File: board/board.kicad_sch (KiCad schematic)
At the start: 8 parts, among them J1 020_1000BASE-T_with_CT, J2 003_power, J3 008_USB, J4 001_I2C, J5 008_USB, J6 002_SPI, J7 010_UART

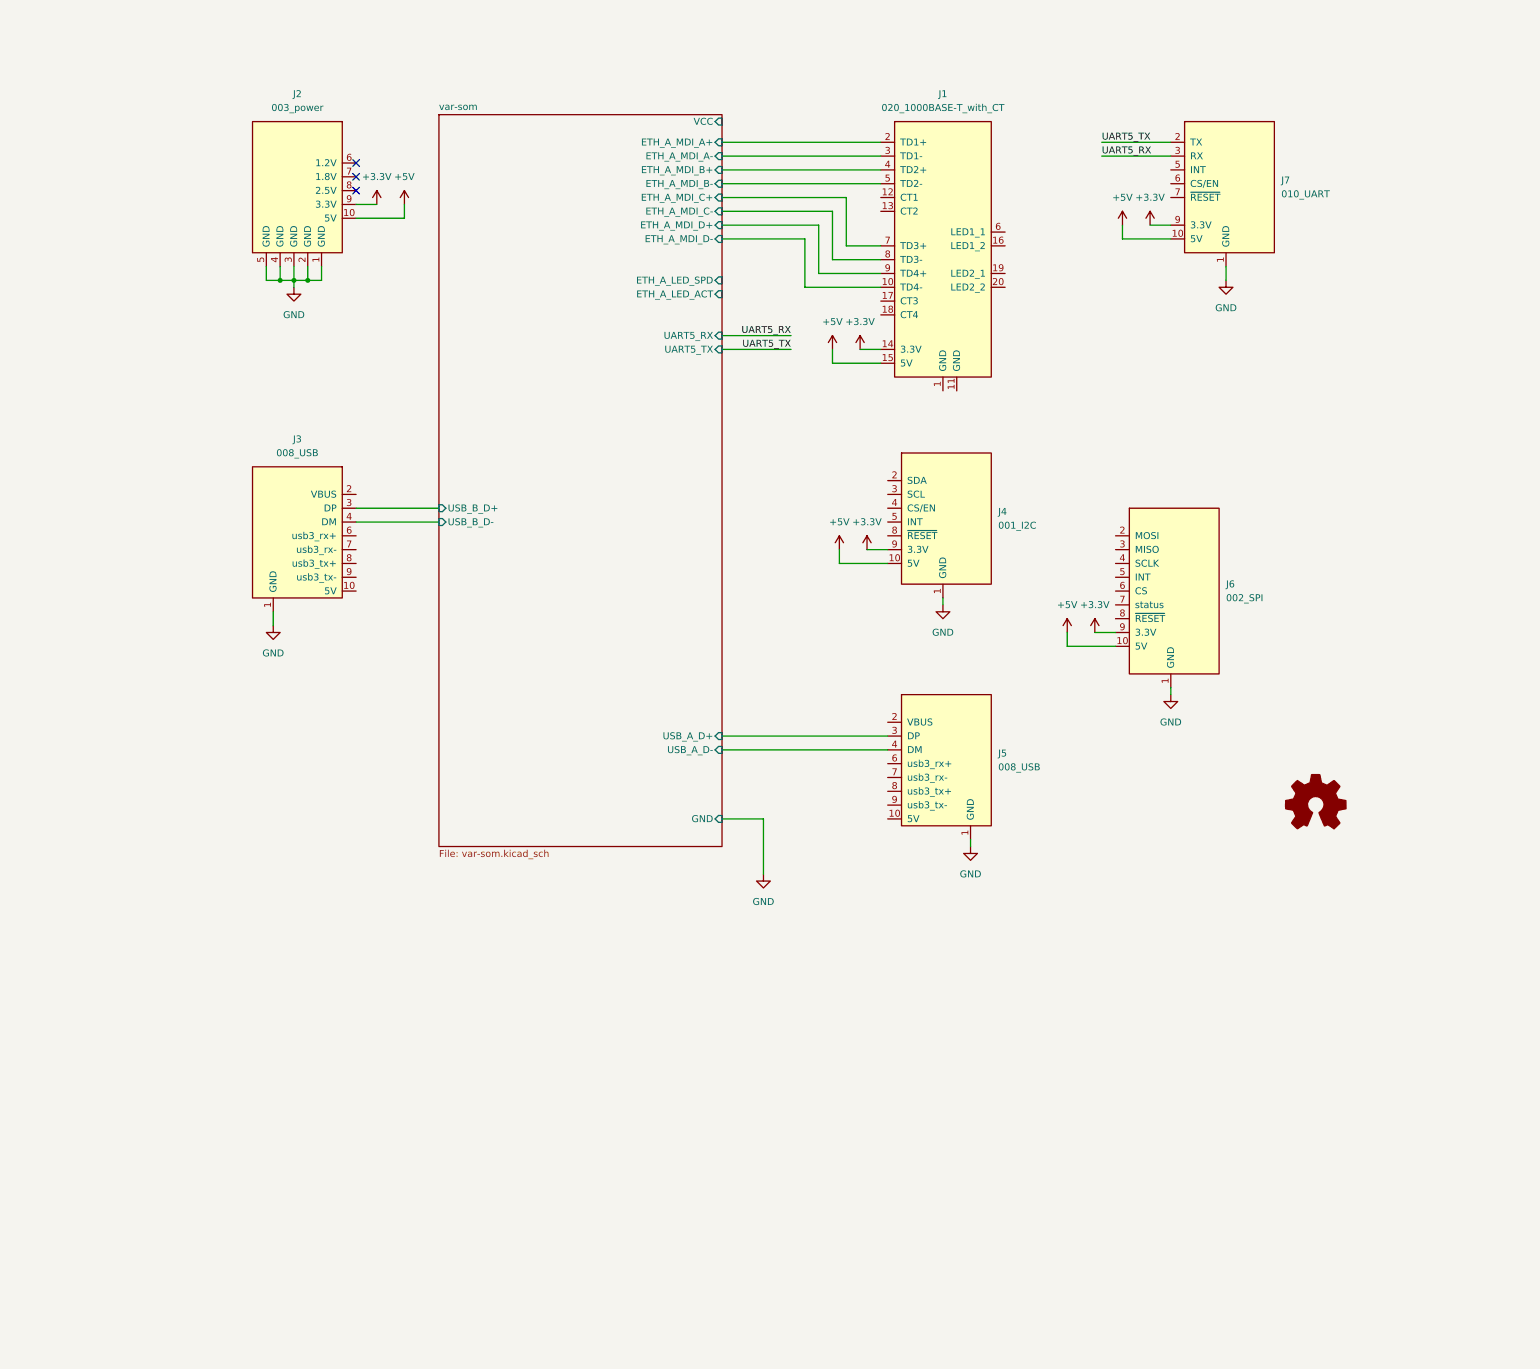
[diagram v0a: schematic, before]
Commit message: added RGMII interface
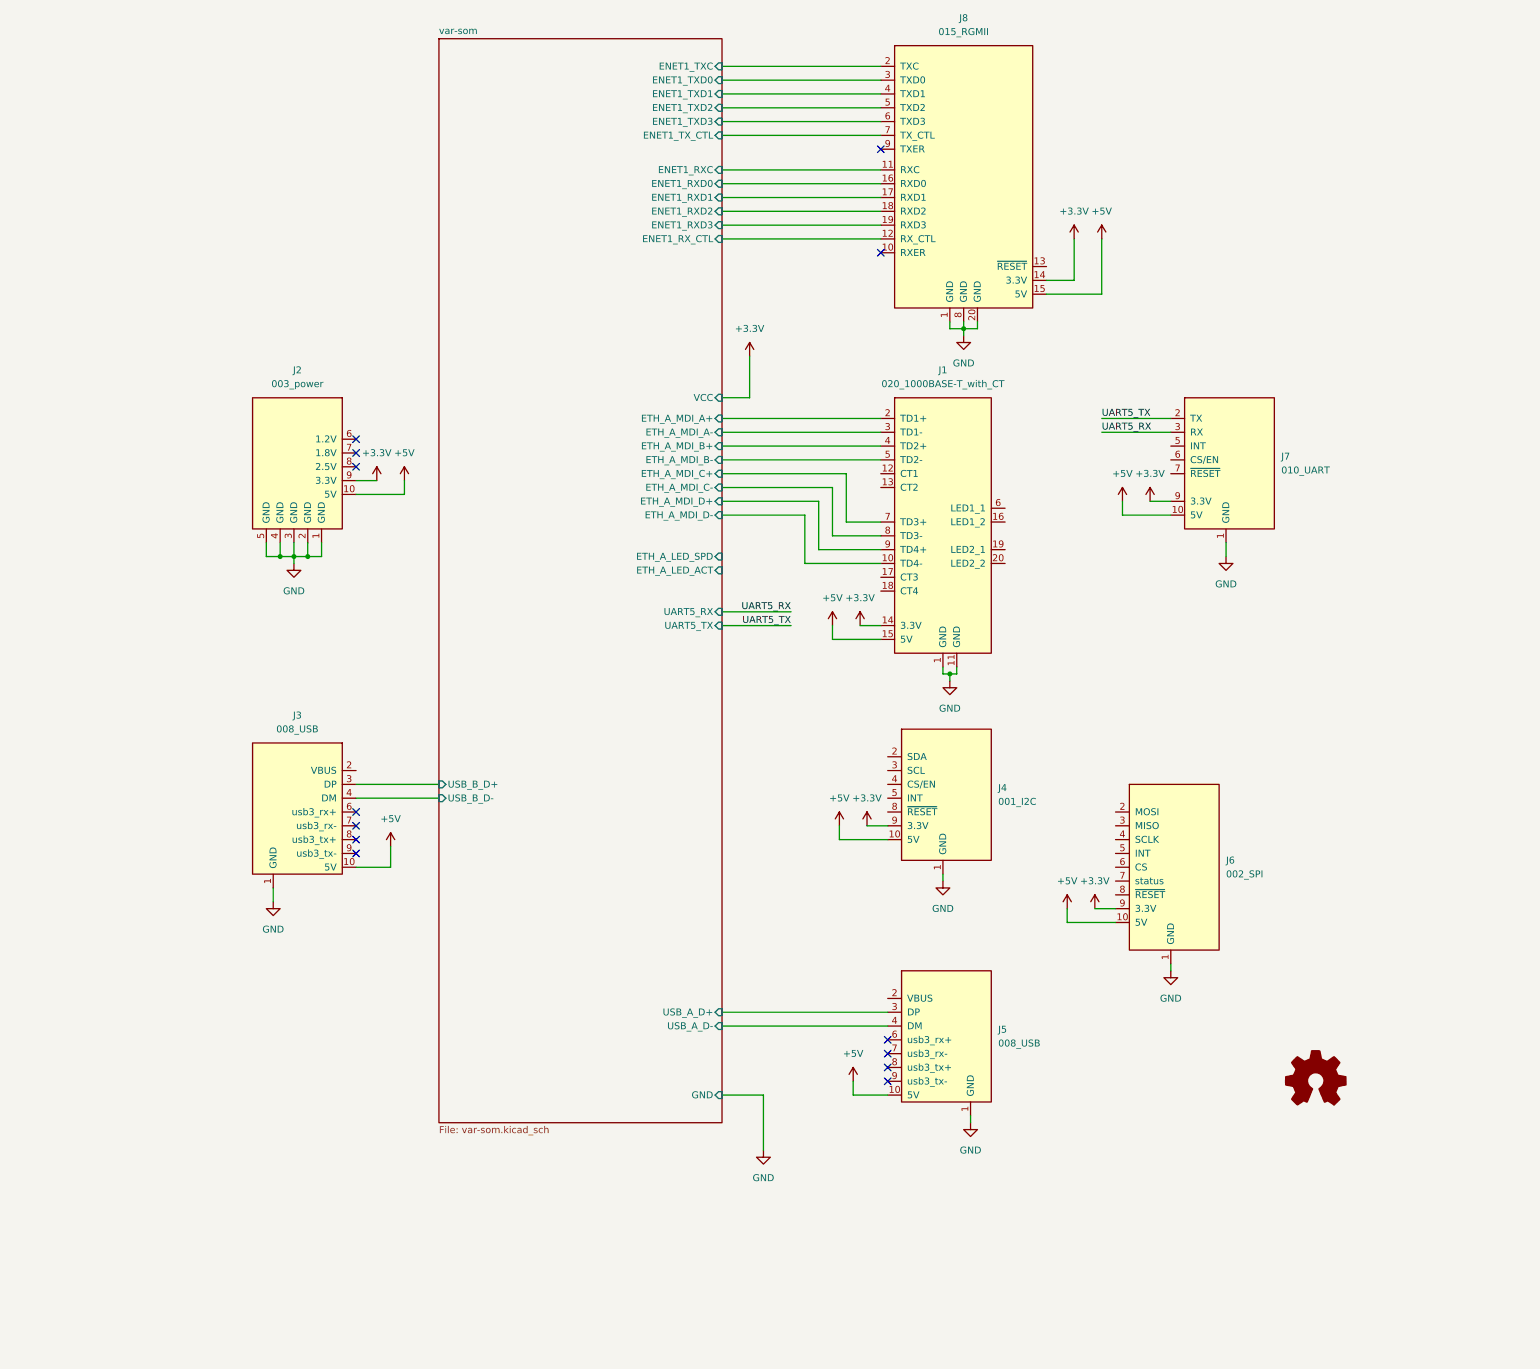
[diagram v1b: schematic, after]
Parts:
- added J8: 015_RGMII, on_edge:on_edge_2x10_host, symbol put_on_edge:015_RGMII
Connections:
- net +3.3V: now also J8.14 (3.3V)
- net +5V: now also J3.10 (5V), J5.10 (5V), J8.15 (5V)
- net GND: now also J1.1 (GND), J1.11 (GND), J8.1 (GND), J8.20 (GND), J8.8 (GND)
- new net var-som/ENET1_RXC: J8.11 (RXC)
- new net var-som/ENET1_RXD0: J8.16 (RXD0)
- new net var-som/ENET1_RXD1: J8.17 (RXD1)
- new net var-som/ENET1_RXD2: J8.18 (RXD2)
- new net var-som/ENET1_RXD3: J8.19 (RXD3)
- new net var-som/ENET1_RX_CTL: J8.12 (RX_CTL)
- new net var-som/ENET1_TXC: J8.2 (TXC)
- new net var-som/ENET1_TXD0: J8.3 (TXD0)
- new net var-som/ENET1_TXD1: J8.4 (TXD1)
- new net var-som/ENET1_TXD2: J8.5 (TXD2)
- new net var-som/ENET1_TXD3: J8.6 (TXD3)
- new net var-som/ENET1_TX_CTL: J8.7 (TX_CTL)
- no-connect marks 3 -> 13
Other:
- sheet var-som ports: added ENET1_RXC, ENET1_RXD0, ENET1_RXD1, ENET1_RXD2, ENET1_RXD3, ENET1_RX_CTL, ENET1_TXC, ENET1_TXD0, ENET1_TXD1, ENET1_TXD2, ENET1_TXD3, ENET1_TX_CTL; removed none
- moved on the sheet: J1, J2, J3, J4, J5, J6, J7

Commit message: added uSD card
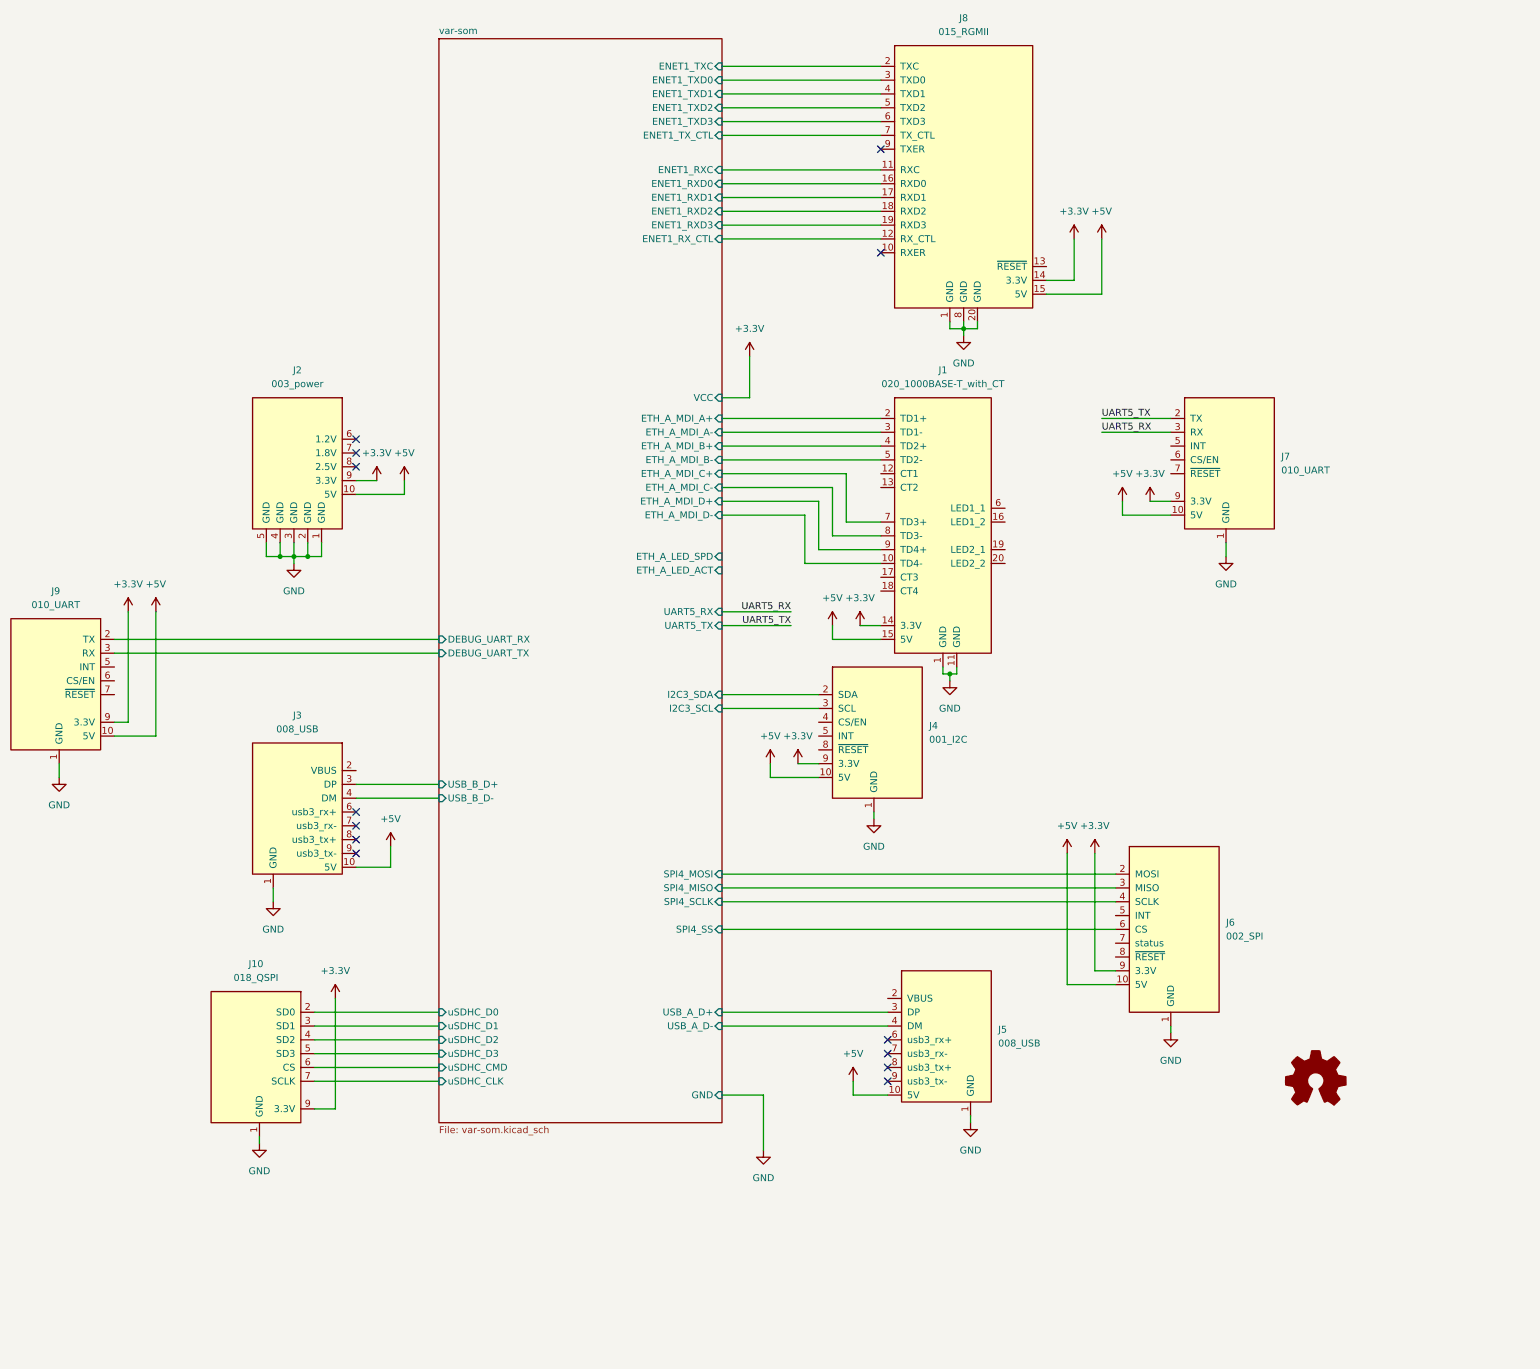
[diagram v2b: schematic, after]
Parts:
- added J10: 018_QSPI, on_edge:on_edge_2x05_device, symbol put_on_edge:018_QSPI
- added J9: 010_UART, on_edge:on_edge_2x05_device, symbol put_on_edge:010_UART
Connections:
- net +3.3V: now also J10.9 (3.3V), J9.9 (3.3V)
- net +5V: now also J9.10 (5V)
- net GND: now also J10.1 (GND), J9.1 (GND)
- net var-som/I2C3_SDA: now reaches J4.2 (SDA)
- net var-som/I2C3_SCL: now reaches J4.3 (SCL)
- net var-som/SPI4_MOSI: now reaches J6.2 (MOSI)
- net var-som/SPI4_MISO: now reaches J6.3 (MISO)
- net var-som/SPI4_SCLK: now reaches J6.4 (SCLK)
- net var-som/SPI4_SS: now reaches J6.6 (CS)
- new net var-som/DEBUG_UART_RX: J9.2 (TX)
- new net var-som/DEBUG_UART_TX: J9.3 (RX)
- new net var-som/uSDHC_CLK: J10.7 (SCLK)
- new net var-som/uSDHC_CMD: J10.6 (CS)
- new net var-som/uSDHC_D0: J10.2 (SD0)
- new net var-som/uSDHC_D1: J10.3 (SD1)
- new net var-som/uSDHC_D2: J10.4 (SD2)
- new net var-som/uSDHC_D3: J10.5 (SD3)
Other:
- sheet var-som ports: added DEBUG_UART_RX, DEBUG_UART_TX, I2C3_SCL, I2C3_SDA, SPI4_MISO, SPI4_MOSI, SPI4_SCLK, SPI4_SS, uSDHC_CLK, uSDHC_CMD, uSDHC_D0, uSDHC_D1, uSDHC_D2, uSDHC_D3; removed none
- moved on the sheet: J4, J6

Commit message: added 1.8v power option for RGMII IO
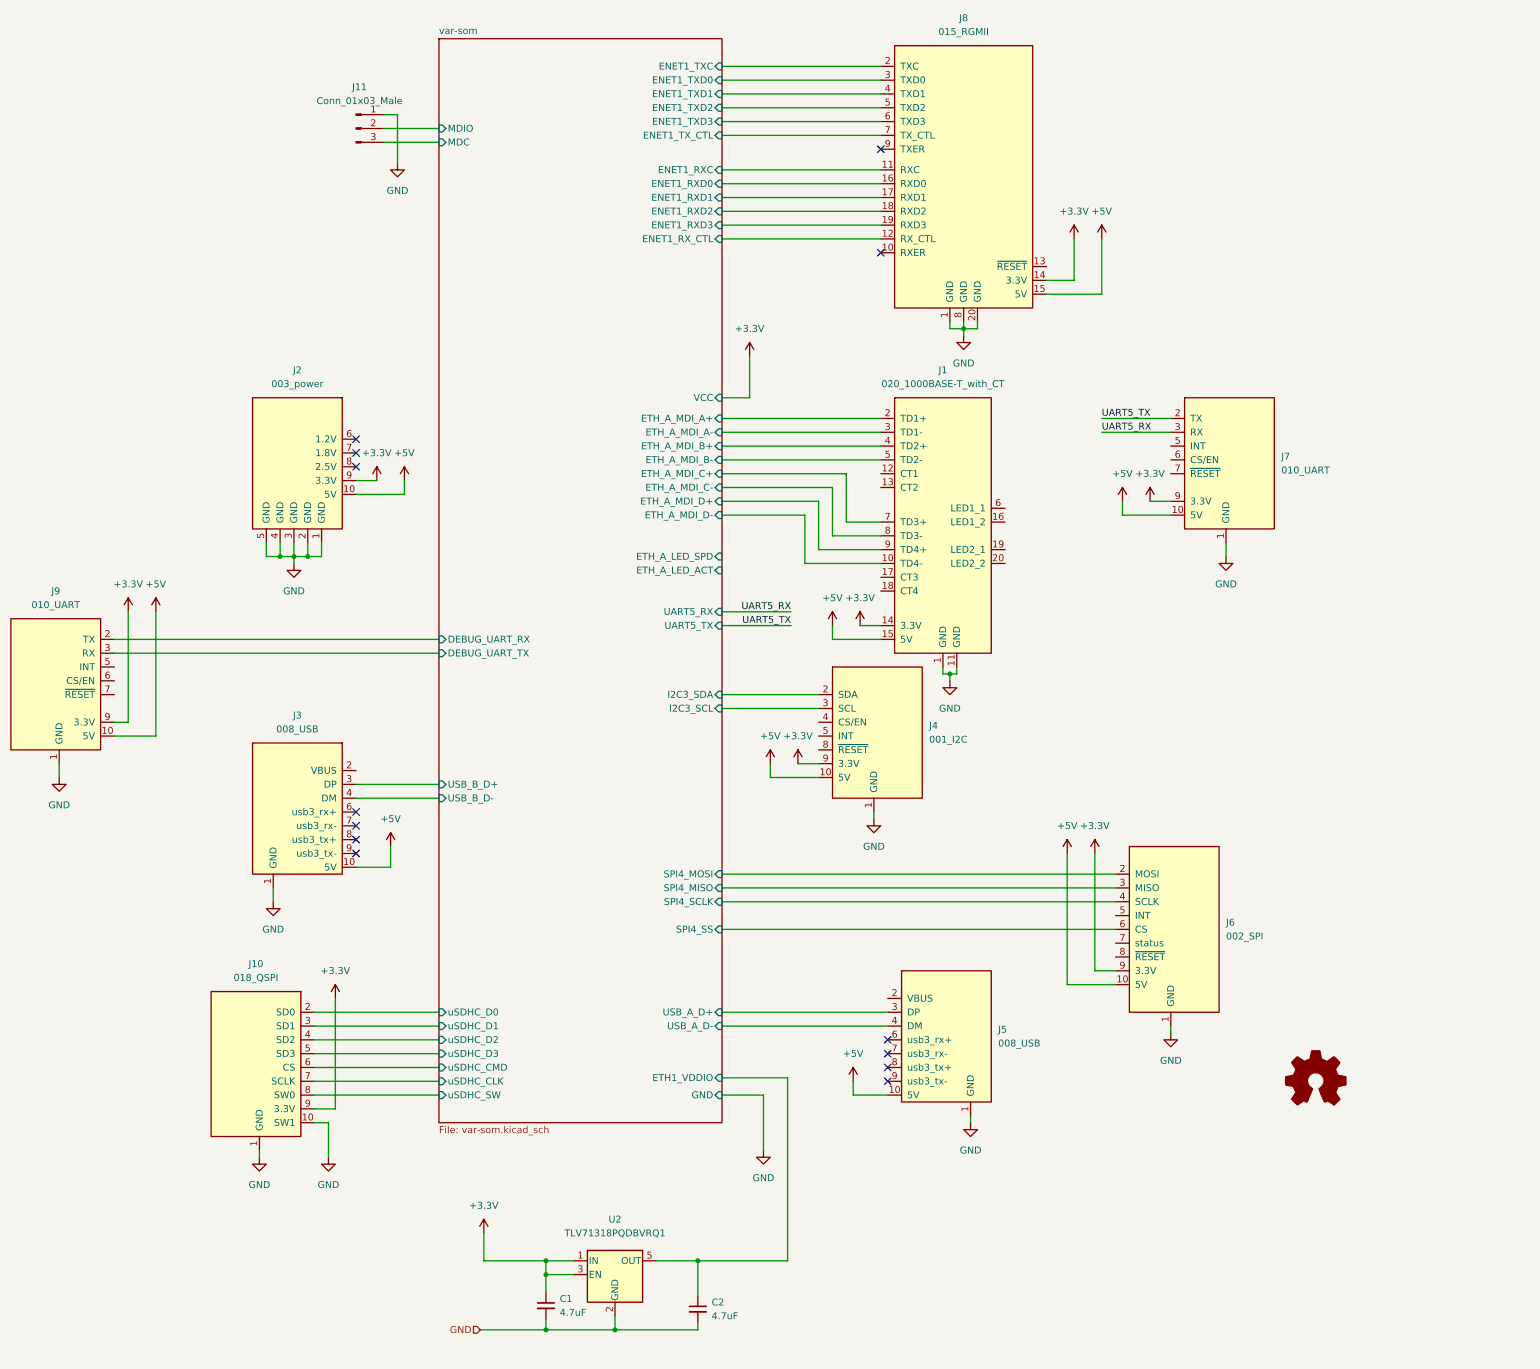
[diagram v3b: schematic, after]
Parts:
- added C1, C2: 4.7uF, Capacitor_SMD:C_0603_1608Metric, symbol Device:C_Small
- added J11: Conn_01x03_Male, Connector_PinSocket_2.54mm:PinSocket_1x03_P2.54mm_Vertical, symbol Connector:Conn_01x03_Male
- added U2: TLV71318PQDBVRQ1, Package_TO_SOT_SMD:SOT-23-5, symbol Regulator_Linear:TLV71209_SOT23-5
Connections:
- net +3.3V: now also C1.1, U2.1 (IN), U2.3 (EN)
- net GND: now also J10.10 (SW1), C1.2, C2.2, J11.1 (Pin_1), U2.2 (GND)
- new net var-som/ETH1_VDDIO: C2.1, U2.5 (OUT)
- new net var-som/MDC: J11.3 (Pin_3)
- new net var-som/MDIO: J11.2 (Pin_2)
- new net var-som/uSDHC_SW: J10.8 (SW0)
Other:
- sheet var-som ports: added ETH1_VDDIO, MDC, MDIO, uSDHC_SW; removed none
